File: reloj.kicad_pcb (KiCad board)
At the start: 2 copper layers, 125 x 102.5 mm, 89 parts, among them J1 Conn_01x03, J2 USB_B_Mini, SW1 SW_Push, SW2 SW_Push, U1 LM555, U10 74LS90, U11 74LS92, U12 74LS90, U13 74LS08, U14 74LS90, U15 74LS47, U16 74LS47, U17 74LS47, U18 74LS47, U19 SA04-11SRWA, U2 74LS90, U20 SA04-11SRWA, U21 SA04-11SRWA, U22 SA04-11SRWA, U3 74LS90, U4 74LS90, U5 74LS90, U6 CD4060B, U7 74LS90, U8 74LS90, U9 74LS92, Y1 32768Hz

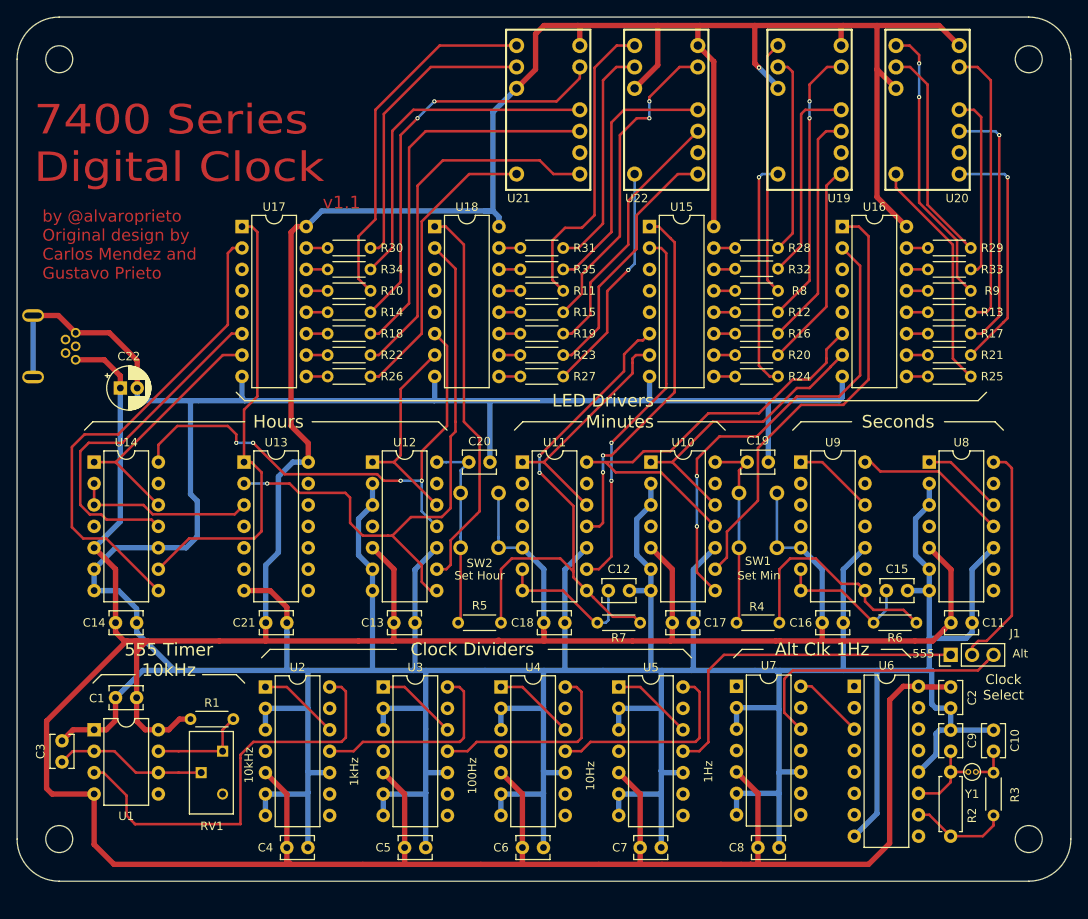
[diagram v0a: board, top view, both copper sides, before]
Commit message: Update layout with v1.2 fixes
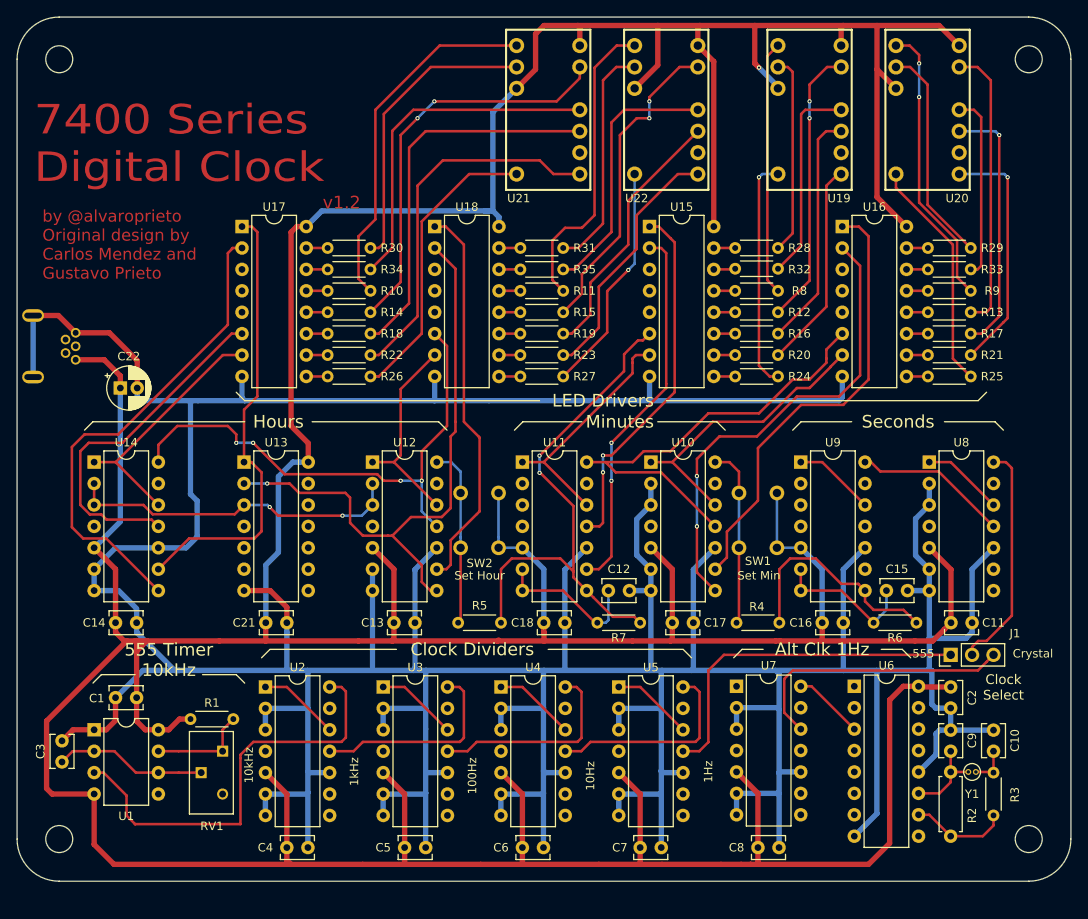
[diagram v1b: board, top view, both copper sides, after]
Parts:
- removed C19, C20: 0.1u, Capacitor_THT:C_Disc_D3.8mm_W2.6mm_P2.50mm
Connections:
- U12 pad 2: GND -> /H_RST
- U12 pad 3: GND -> /H_RST
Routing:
- net GND: track 698.3 -> 672.1 mm
- net /H_RST: track 21.2 -> 40.1 mm, vias 0 -> 2
- net /CLK_HR: track 23.3 -> 21.3 mm
- net /CLK_MIN: track 23.4 -> 21.4 mm
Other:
- board text added: "Crystal"
- board text added: "v1.2"
- board text removed: "Alt"
- board text removed: "v1.1"

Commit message: Switch to groun pour on botom layer
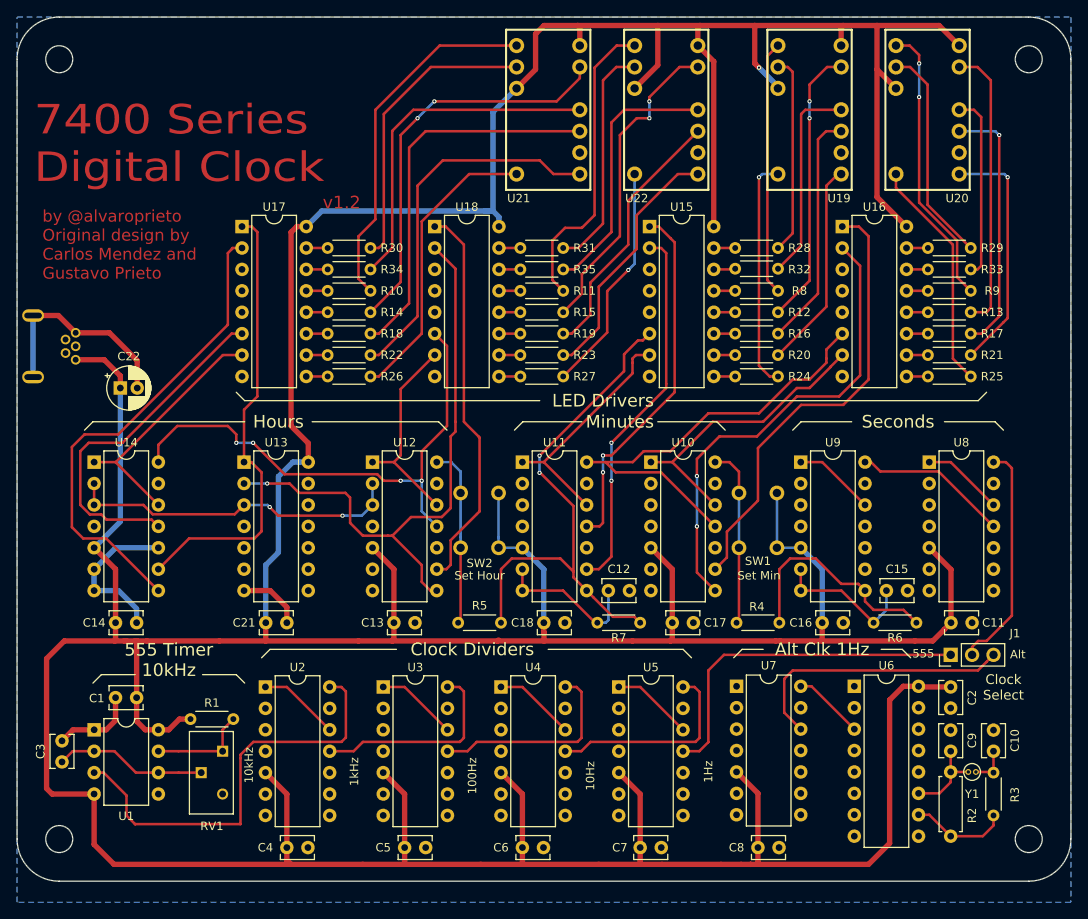
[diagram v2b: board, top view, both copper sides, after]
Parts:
- added REF**: OSHW-Logo_11.4x12mm_SilkScreen, Symbol:OSHW-Logo_11.4x12mm_SilkScreen, B.Cu at (109.0, 58.0)
- R1: value 220 -> 330
- R10, R11, R12, R13, R14, R15, R16, R17, R18, R19, R20, R21, R22, R23, R24, R25, R26, R27, R28, R29, R30, R31, R32, R33, R34, R35, R8, R9: value 330 -> 1k
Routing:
- net GND: track 672.1 -> 61.7 mm
- net CA: track 680.2 -> 682.1 mm
- added copper zone on B.Cu, net GND
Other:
- board text added: "Alt"
- board text removed: "Crystal"
